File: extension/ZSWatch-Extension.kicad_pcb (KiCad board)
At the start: 4 copper layers, 16.8 x 16.8 mm, 37 parts, among them IC501 MAX32664, IC502 LIS2DS12, IC503 MAX86141, IC601 DA7212-01UM2, X701 MB2, X702 MB1, Y501 32kHz

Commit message: Add power rail test points and mounting orientation arrow
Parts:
- added HR: 1V8_HR, TestPoint:TestPoint_Pad_D1.0mm, B.Cu at (199.0, 154.1)
- added PA: 1V8_PA, TestPoint:TestPoint_Pad_D1.0mm, B.Cu at (206.1, 156.9)
- added V: VSYS, TestPoint:TestPoint_Pad_D1.0mm, B.Cu at (198.3, 148.4)
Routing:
- net /Project Architecture/Connectors/+1V8_HR: track 11.6 -> 15.1 mm
- net VSYS: track 33.4 -> 36.5 mm
- net /Project Architecture/Audio/+1V8_PA: track 2.02 -> 2.99 mm

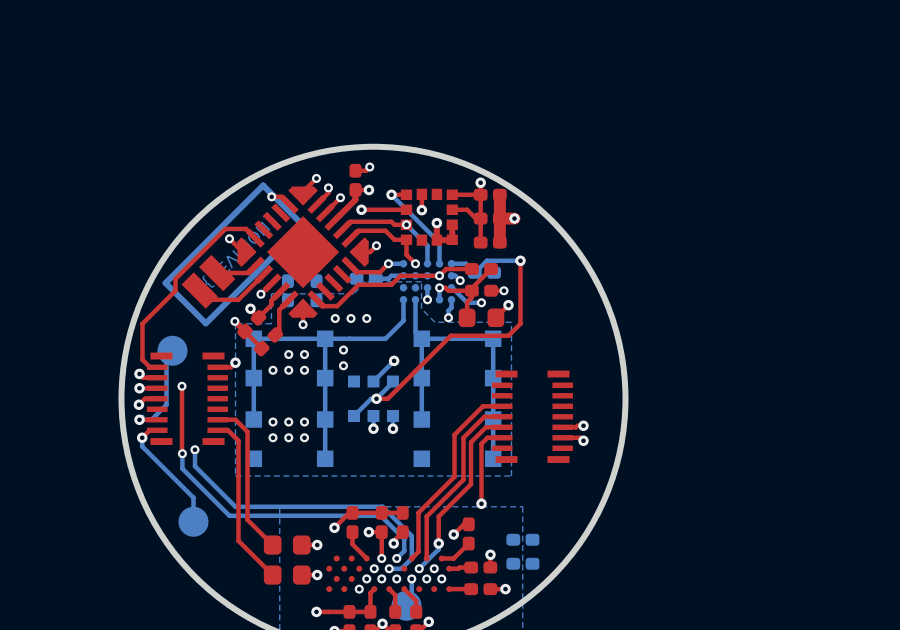
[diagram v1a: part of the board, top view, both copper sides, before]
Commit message: Bug: Issue #3
- Replace VLED capacitor with 10 V type

Closes: #3

Signed-off-by: Daniel Kampert <DanielKampert@kampis-elektroecke.de>
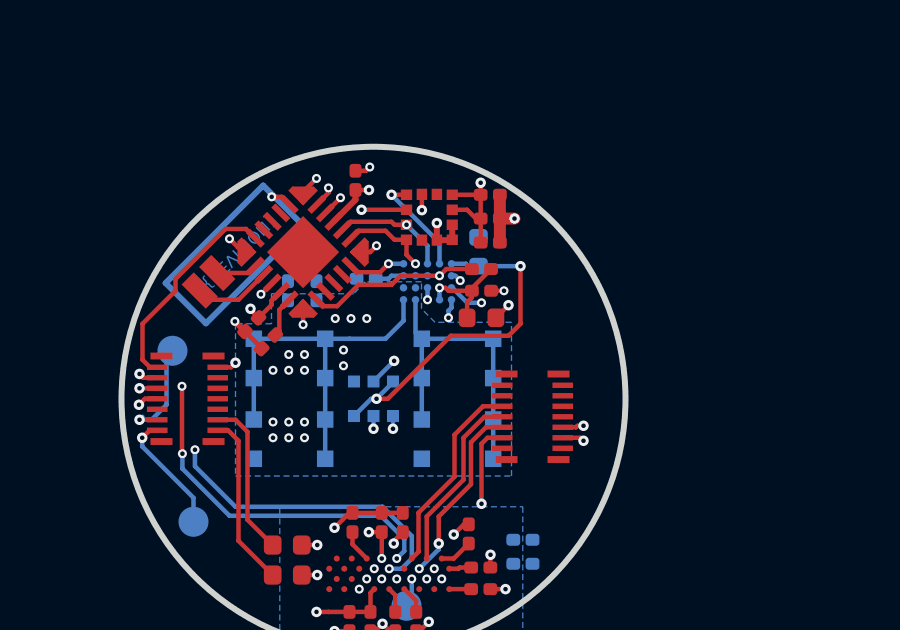
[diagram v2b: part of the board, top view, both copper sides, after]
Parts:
- C508: footprint Capacitor_SMD:C_0201_0603Metric -> Capacitor_SMD:C_0402_1005Metric
- moved C508 0.73 mm to (208.5, 145.1), turned to 90 degrees
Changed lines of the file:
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@@
 		(embedded_fonts no)
 	)
-	(footprint "Capacitor_SMD:C_0201_0603Metric"
+	(footprint "Capacitor_SMD:C_0402_1005Metric"
 		(layer "B.Cu")
-		(at 208.7 145.8)
-		(descr "Capacitor SMD 0201 (0603 Metric), square (rectangular) end terminal, IPC-7351 nominal, (Body size source: https://www.vishay.com/docs/20052/crcw0201e3.pdf), generated with kicad-footprint-generator")
+		(at 208.5 145.1 90)
+		(descr "Capacitor SMD 0402 (1005 Metric), square (rectangular) end terminal, IPC-7351 nominal, (Body size source: IPC-SM-782 page 76, https://www.pcb-3d.com/wordpress/wp-content/uploads/ipc-sm-782a_amendment_1_and_2.pdf), generated with kicad-footprint-generator")
 		(tags "capacitor")
 		(property "Reference" "C508"
-			(at 0 1.05 0)
+			(at 0 1.16 90)
 			(layer "B.SilkS")
 			(hide yes)
@@
 		)
 		(property "Value" "10u"
-			(at 0 -1.05 0)
+			(at 0 -1.16 90)
 			(layer "B.Fab")
 			(hide yes)
@@
 			)
 		)
-		(property "Datasheet" "https://datasheets.kyocera-avx.com/cx5r-KGM.pdf"
-			(at 0 0 0)
+		(property "Datasheet" ""
+			(at 0 0 90)
 			(layer "B.Fab")
 			(hide yes)
@@
 			)
 		)
-		(property "Description" "Unpolarized capacitor, small symbol"
-			(at 0 0 0)
+		(property "Description" ""
+			(at 0 0 90)
 			(layer "B.Fab")
 			(hide yes)
@@
 			)
 		)
-		(property "CONFIG" ""
-			(at 0 0 180)
-			(unlocked yes)
-			(layer "B.Fab")
-			(hide yes)
-			(effects
-				(font
-					(size 0.8 0.8)
-					(thickness 0.12)
-				)
-				(justify mirror)
-			)
-		)
-		(property "manf" "KYOCERA AVX"
-			(at 0 0 180)
-			(unlocked yes)
-			(layer "B.Fab")
-			(hide yes)
-			(effects
-				(font
-					(size 0.8 0.8)
-					(thickness 0.12)
-				)
-				(justify mirror)
-			)
-		)
-		(property "manf#" "KGM03DR50G106MH"
-			(at 0 0 180)
-			(unlocked yes)
-			(layer "B.Fab")
-			(hide yes)
-			(effects
-				(font
-					(size 0.8 0.8)
-					(thickness 0.12)
-				)
-				(justify mirror)
-			)
-		)
-		(property "mouser#" "581-KGM03DR50G106MH"
-			(at 0 0 180)
-			(unlocked yes)
-			(layer "B.Fab")
-			(hide yes)
-			(effects
-				(font
-					(size 0.8 0.8)
-					(thickness 0.12)
-				)
-				(justify mirror)
-			)
-		)
 		(property ki_fp_filters "C_*")
 		(sheetname "/Project Architecture/Heartrate/")
@@
 		(attr smd)
 		(fp_line
-			(start -0.7 -0.35)
-			(end -0.7 0.35)
+			(start -0.107836 -0.36)
+			(end 0.107836 -0.36)
+			(stroke
+				(width 0.12)
+				(type solid)
+			)
+			(layer "B.SilkS")
+		)
+		(fp_line
+			(start -0.107836 0.36)
+			(end 0.107836 0.36)
+			(stroke
+				(width 0.12)
+				(type solid)
+			)
+			(layer "B.SilkS")
+		)
+		(fp_line
+			(start 0.91 -0.46)
+			(end -0.91 -0.46)
 			(stroke
 				(width 0.05)
@@
 		)
 		(fp_line
-			(start -0.7 0.35)
-			(end 0.7 0.35)
+			(start -0.91 -0.46)
+			(end -0.91 0.46)
 			(stroke
 				(width 0.05)
@@
 		)
 		(fp_line
-			(start 0.7 -0.35)
-			(end -0.7 -0.35)
+			(start 0.91 0.46)
+			(end 0.91 -0.46)
 			(stroke
 				(width 0.05)
@@
 		)
 		(fp_line
-			(start 0.7 0.35)
-			(end 0.7 -0.35)
+			(start -0.91 0.46)
+			(end 0.91 0.46)
 			(stroke
 				(width 0.05)
@@
 		)
 		(fp_line
-			(start -0.3 -0.15)
-			(end -0.3 0.15)
+			(start 0.5 -0.25)
+			(end -0.5 -0.25)
 			(stroke
 				(width 0.1)
@@
 		)
 		(fp_line
-			(start -0.3 0.15)
-			(end 0.3 0.15)
+			(start -0.5 -0.25)
+			(end -0.5 0.25)
 			(stroke
 				(width 0.1)
@@
 		)
 		(fp_line
-			(start 0.3 -0.15)
-			(end -0.3 -0.15)
+			(start 0.5 0.25)
+			(end 0.5 -0.25)
 			(stroke
 				(width 0.1)
@@
 		)
 		(fp_line
-			(start 0.3 0.15)
-			(end 0.3 -0.15)
+			(start -0.5 0.25)
+			(end 0.5 0.25)
 			(stroke
 				(width 0.1)
@@
 		)
 		(fp_text user "${REFERENCE}"
-			(at 0.02 0 0)
+			(at 0 0 90)
 			(layer "B.Fab")
 			(effects
@@
 			)
 		)
-		(pad "" smd roundrect
-			(at -0.345 0)
-			(size 0.318 0.36)
-			(layers "B.Paste")
-			(roundrect_rratio 0.25)
-		)
-		(pad "" smd roundrect
-			(at 0.345 0)
-			(size 0.318 0.36)
-			(layers "B.Paste")
-			(roundrect_rratio 0.25)
-		)
 		(pad "1" smd roundrect
-			(at -0.32 0)
-			(size 0.46 0.4)
-			(layers "B.Cu" "B.Mask")
+			(at -0.48 0 90)
+			(size 0.56 0.62)
+			(layers "B.Cu" "B.Mask" "B.Paste")
 			(roundrect_rratio 0.25)
 			(net 4 "VSYS")
@@
 		)
 		(pad "2" smd roundrect
-			(at 0.32 0)
-			(size 0.46 0.4)
-			(layers "B.Cu" "B.Mask")
+			(at 0.48 0 90)
+			(size 0.56 0.62)
+			(layers "B.Cu" "B.Mask" "B.Paste")
 			(roundrect_rratio 0.25)
 			(net 1 "GND")
@@
 		)
 		(embedded_fonts no)
-		(model "${KICAD9_3DMODEL_DIR}/Capacitor_SMD.3dshapes/C_0201_0603Metric.step"
+		(model "${KICAD9_3DMODEL_DIR}/Capacitor_SMD.3dshapes/C_0402_1005Metric.step"
 			(offset
 				(xyz 0 0 0)
@@
 			(justify left)
 		)
-		(render_cache "   " 0)
+		(render_cache "   " 0
+			(polygon
+				(pts
+					(xy 26.4 128.415)
+				)
+			)
+			(polygon
+				(pts
+					(xy 27.8 128.415)
+				)
+			)
+			(polygon
+				(pts
+					(xy 29.2 128.415)
+				)
+			)
+		)
 	)
 	(gr_text "   "
@@
 			(justify left)
 		)
-		(render_cache "   " 0)
+		(render_cache "   " 0
+			(polygon
+				(pts
+					(xy 26.4 131.415)
+				)
+			)
+			(polygon
+				(pts
+					(xy 27.8 131.415)
+				)
+			)
+			(polygon
+				(pts
+					(xy 29.2 131.415)
+				)
+			)
+		)
 	)
 	(gr_text ""
@@
 			(keep_text_aligned yes)
 		)
-		(gr_text "16.8000 mm"
+		(gr_text "16,8000 mm"
 			(at 205 162.58 0)
 			(layer "User.6")
@@
 			(keep_text_aligned yes)
 		)
-		(gr_text "16.8000 mm"
+		(gr_text "16,8000 mm"
 			(at 218.08 150 90)
 			(layer "User.6")
@@
 	)
 	(segment
-		(start 209.5 147.9)
-		(end 209.9 147.5)
-		(width 0.15)
-		(layer "F.Cu")
-		(net 4)
-	)
-	(segment
 		(start 203.500001 157.105001)
 		(end 204.2 157.105)
@@
 	)
 	(segment
-		(start 207.57748 147.9)
-		(end 209.5 147.9)
-		(width 0.15)
-		(layer "F.Cu")
-		(net 4)
-	)
-	(segment
-		(start 205.1 150)
-		(end 205.47748 150)
-		(width 0.15)
-		(layer "F.Cu")
-		(net 4)
-	)
-	(segment
 		(start 204.9 156.47)
 		(end 204.9 157.105)
@@
 	)
 	(segment
-		(start 205.47748 150)
-		(end 207.57748 147.9)
-		(width 0.15)
-		(layer "F.Cu")
-		(net 4)
-	)
-	(segment
-		(start 209.9 147.5)
-		(end 209.9 145.4)
-		(width 0.15)
-		(layer "F.Cu")
-		(net 4)
-	)
-	(segment
 		(start 205.025 156.345)
 		(end 204.9 156.47)
@@
 	)
 	(via
-		(at 209.9 145.4)
+		(at 209.9 145.58)
 		(size 0.35)
 		(drill 0.15)
@@
 	)
 	(segment
-		(start 207.6 145.5)
-		(end 208.08 145.5)
-		(width 0.15)
-		(layer "B.Cu")
-		(net 4)
-	)
-	(segment
-		(start 208.08 145.5)
-		(end 208.38 145.8)
-		(width 0.15)
-		(layer "B.Cu")
-		(net 4)
-	)
-	(segment
 		(start 198.1 148.6)
 		(end 198.3 148.4)
@@
 	)
 	(segment
-		(start 209.9 145.4)
-		(end 208.78 145.4)
-		(width 0.15)
-		(layer "B.Cu")
-		(net 4)
-	)
-	(segment
-		(start 208.78 145.4)
-		(end 208.38 145.8)
-		(width 0.15)
-		(layer "B.Cu")
-		(net 4)
-	)
-	(segment
 		(start 197.4 152.5)
 		(end 202.005 157.105)
@@
 	)
 	(embedded_fonts no)
+	(segment
+		(start 209.9 145.58)
+		(end 209.9 147.5)
+		(width 0.15)
+		(layer "F.Cu")
+		(net 4)
+	)
+	(segment
+		(start 209.5 147.9)
+		(end 207.57748 147.9)
+		(width 0.15)
+		(layer "F.Cu")
+		(net 4)
+	)
+	(segment
+		(start 207.57748 147.9)
+		(end 205.47748 150)
+		(width 0.15)
+		(layer "F.Cu")
+		(net 4)
+	)
+	(segment
+		(start 209.9 147.5)
+		(end 209.5 147.9)
+		(width 0.15)
+		(layer "F.Cu")
+		(net 4)
+	)
+	(segment
+		(start 205.47748 150)
+		(end 205.1 150)
+		(width 0.15)
+		(layer "F.Cu")
+		(net 4)
+	)
+	(segment
+		(start 208.08 145.5)
+		(end 207.6 145.5)
+		(width 0.15)
+		(layer "B.Cu")
+		(net 4)
+	)
+	(segment
+		(start 209.9 145.58)
+		(end 208.16 145.58)
+		(width 0.15)
+		(layer "B.Cu")
+		(net 4)
+	)
+	(segment
+		(start 208.16 145.58)
+		(end 208.08 145.5)
+		(width 0.15)
+		(layer "B.Cu")
+		(net 4)
+	)
 )
